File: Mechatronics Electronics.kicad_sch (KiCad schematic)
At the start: 2 parts

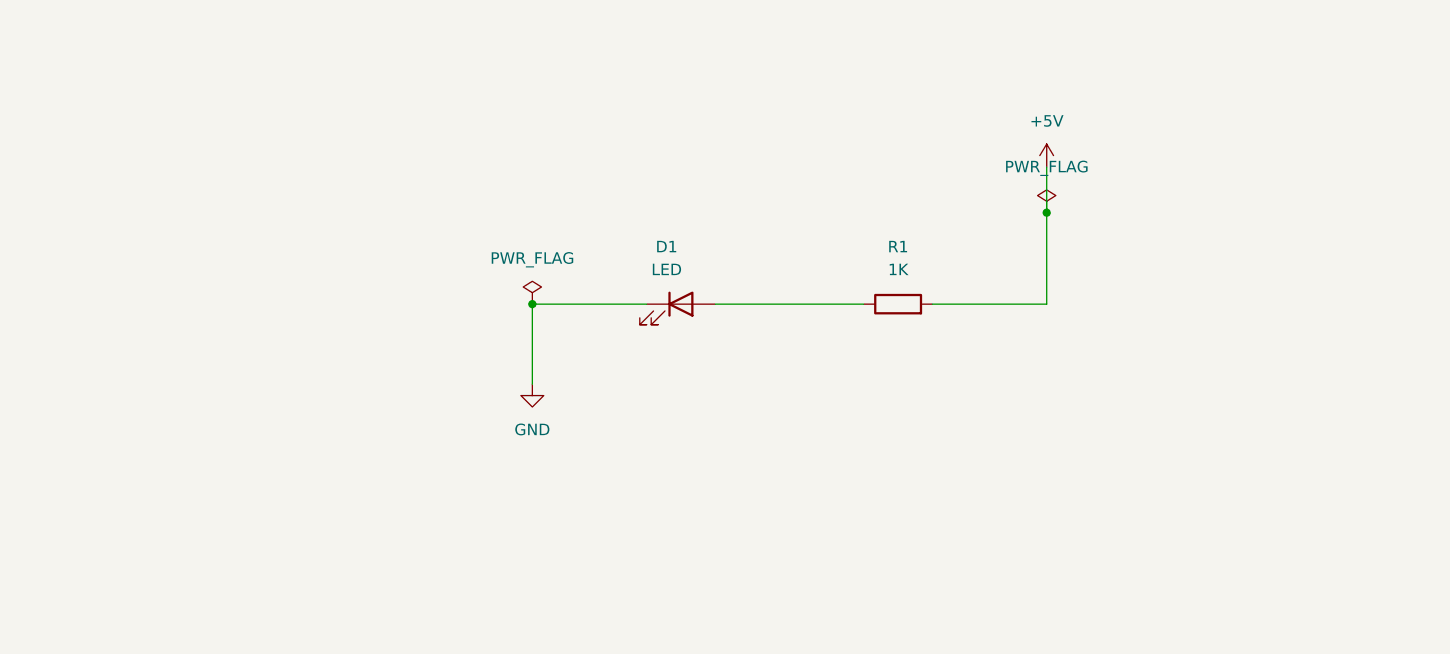
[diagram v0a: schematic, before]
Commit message: Added TCAN4551-Q1 custom footprint/symbol and applied BGA microvia DRC rule
- Created and linked custom symbol + footprint for TCAN4551-Q1
- Added KiCad default MCIMX6D4AVT symbol
- Defined BGA_Area rule with microvia geometry:
  * Min annular width: 2 mil
  * Min via diameter: 8 mil
  * Min via hole size: 4 mil
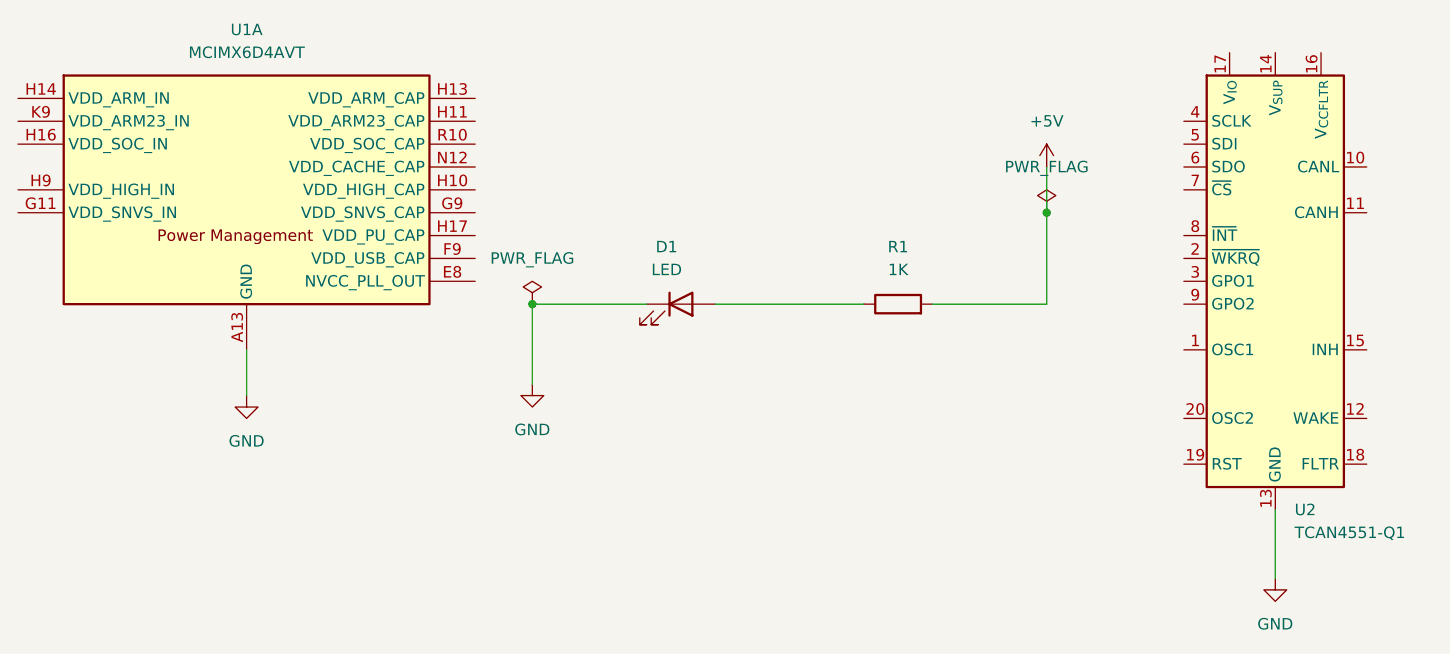
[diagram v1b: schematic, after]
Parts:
- added U1: MCIMX6D4AVT, Package_BGA:BGA-624_21x21mm_Layout25x25_P0.8mm, symbol CPU_NXP_IMX:MCIMX6D4AVT
- added U2: TCAN4551-Q1, TCAN_Library:TCAN4551-Q1, symbol TCAN_Library:TCAN4551-Q1
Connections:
- net GND: now also U1.A13 (GND), U1.A25 (GND), U1.A4 (GND), U1.A8 (GND), U1.AA10 (GND), U1.AA13 (GND), U1.AA16 (GND), U1.AA19 (GND), U1.AA22 (GND), U1.AA7 (GND), U1.AB24 (GND), U1.AB3 (GND), U1.AD10 (GND), U1.AD13 (GND), U1.AD16 (GND), U1.AD19 (GND), U1.AD22 (GND), U1.AD4 (GND), U1.AD7 (GND), U1.AE1 (GND), U1.AE25 (GND), U1.B4 (GND), U1.C1 (GND), U1.C10 (GND), U1.C4 (GND), U1.C6 (GND), U1.D3 (GND), U1.D6 (GND), U1.D8 (GND), U1.E5 (GND), U1.E6 (GND), U1.E7 (GND), U1.F5 (GND), U1.F6 (GND), U1.F7 (GND), U1.F8 (GND), U1.G10 (GND), U1.G19 (GND), U1.G3 (GND), U1.H12 (GND), U1.H15 (GND), U1.H18 (GND), U1.H8 (GND), U1.J12 (GND), U1.J15 (GND), U1.J18 (GND), U1.J2 (GND), U1.J8 (GND), U1.K10 (GND), U1.K12 (GND), U1.K15 (GND), U1.K18 (GND), U1.K8 (GND), U1.L10 (GND), U1.L12 (GND), U1.L15 (GND), U1.L18 (GND), U1.L2 (GND), U1.L5 (GND), U1.L8 (GND), U1.M10 (GND), U1.M12 (GND), U1.M15 (GND), U1.M18 (GND), U1.M8 (GND), U1.N10 (GND), U1.N15 (GND), U1.N18 (GND), U1.N8 (GND), U1.P10 (GND), U1.P12 (GND), U1.P15 (GND), U1.P18 (GND), U1.P8 (GND), U1.R12 (GND), U1.R15 (GND), U1.R17 (GND), U1.R8 (GND), U1.T11 (GND), U1.T12 (GND), U1.T15 (GND), U1.T17 (GND), U1.T19 (GND), U1.T8 (GND), U1.U11 (GND), U1.U12 (GND), U1.U15 (GND), U1.U17 (GND), U1.U19 (GND), U1.U8 (GND), U1.V19 (GND), U1.V8 (GND), U1.W10 (GND), U1.W11 (GND), U1.W12 (GND), U1.W13 (GND), U1.W15 (GND), U1.W16 (GND), U1.W17 (GND), U1.W18 (GND), U1.W19 (GND), U1.W3 (GND), U1.W7 (GND), U1.W8 (GND), U1.W9 (GND), U1.Y24 (GND), U1.Y5 (GND), U2.13 (GND), U2.21 (GND)
- new net: U1.H10 (VDD_HIGH_CAP), U1.J10 (VDD_HIGH_CAP)
- new net: U1.H11 (VDD_ARM23_CAP), U1.J11 (VDD_ARM23_CAP), U1.K11 (VDD_ARM23_CAP), U1.L11 (VDD_ARM23_CAP), U1.M11 (VDD_ARM23_CAP), U1.N11 (VDD_ARM23_CAP), U1.P11 (VDD_ARM23_CAP), U1.R11 (VDD_ARM23_CAP)
- new net: U1.H13 (VDD_ARM_CAP), U1.J13 (VDD_ARM_CAP), U1.K13 (VDD_ARM_CAP), U1.L13 (VDD_ARM_CAP), U1.M13 (VDD_ARM_CAP), U1.N13 (VDD_ARM_CAP), U1.P13 (VDD_ARM_CAP), U1.R13 (VDD_ARM_CAP)
- new net: U1.H14 (VDD_ARM_IN), U1.J14 (VDD_ARM_IN), U1.K14 (VDD_ARM_IN), U1.L14 (VDD_ARM_IN), U1.M14 (VDD_ARM_IN), U1.N14 (VDD_ARM_IN), U1.P14 (VDD_ARM_IN), U1.R14 (VDD_ARM_IN)
- new net: U1.H16 (VDD_SOC_IN), U1.J16 (VDD_SOC_IN), U1.K16 (VDD_SOC_IN), U1.L16 (VDD_SOC_IN), U1.M16 (VDD_SOC_IN), U1.N16 (VDD_SOC_IN), U1.P16 (VDD_SOC_IN), U1.R16 (VDD_SOC_IN), U1.T16 (VDD_SOC_IN), U1.U16 (VDD_SOC_IN)
- new net: U1.H17 (VDD_PU_CAP), U1.J17 (VDD_PU_CAP), U1.K17 (VDD_PU_CAP), U1.L17 (VDD_PU_CAP), U1.M17 (VDD_PU_CAP), U1.N17 (VDD_PU_CAP), U1.P17 (VDD_PU_CAP)
- new net: U1.H9 (VDD_HIGH_IN), U1.J9 (VDD_HIGH_IN)
- new net: U1.K9 (VDD_ARM23_IN), U1.L9 (VDD_ARM23_IN), U1.M9 (VDD_ARM23_IN), U1.N9 (VDD_ARM23_IN), U1.P9 (VDD_ARM23_IN), U1.R9 (VDD_ARM23_IN), U1.T9 (VDD_ARM23_IN), U1.U9 (VDD_ARM23_IN)
- new net: U1.R10 (VDD_SOC_CAP), U1.T10 (VDD_SOC_CAP), U1.T13 (VDD_SOC_CAP), U1.T14 (VDD_SOC_CAP), U1.U10 (VDD_SOC_CAP), U1.U13 (VDD_SOC_CAP), U1.U14 (VDD_SOC_CAP)
